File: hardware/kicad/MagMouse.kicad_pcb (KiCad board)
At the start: 4 copper layers, 50 x 95 mm, 183 parts, among them J1 TYPE-C-31-M-12, J2 COIL_L, J3 COIL_M, J4 COIL_R, Q1 2N7002, Q2 2N7002, Q3 2N7002, SW1 RESET, SW2 BOOT, U1 TPD2EUSB30DRTR, U10 ADS7038IRTER, U11 TUSB320LAIRWBR, U12 TPS259470LRPWR, U13 TPS259470LRPWR, U14 SN74LVC2G04DCKR, U15 SN74LVC1G123DCUR, U16 SN74LVC08APWR, U17 SN74LVC08APWR, U18 SN74LVC08APWR, U19 TLV9001IDBVR, U2 TPS62162DSGR, U20 TPD2E2U06DCKR, U3 ESP32-S3-MINI-1-N8, U4 DRV8231ADSGR, U5 DRV8231ADSGR, U6 DRV8231ADSGR, U7 TMAG5253BA2IQDMRR, U8 TMAG5253BA2IQDMRR, U9 TMAG5253BA2IQDMRR

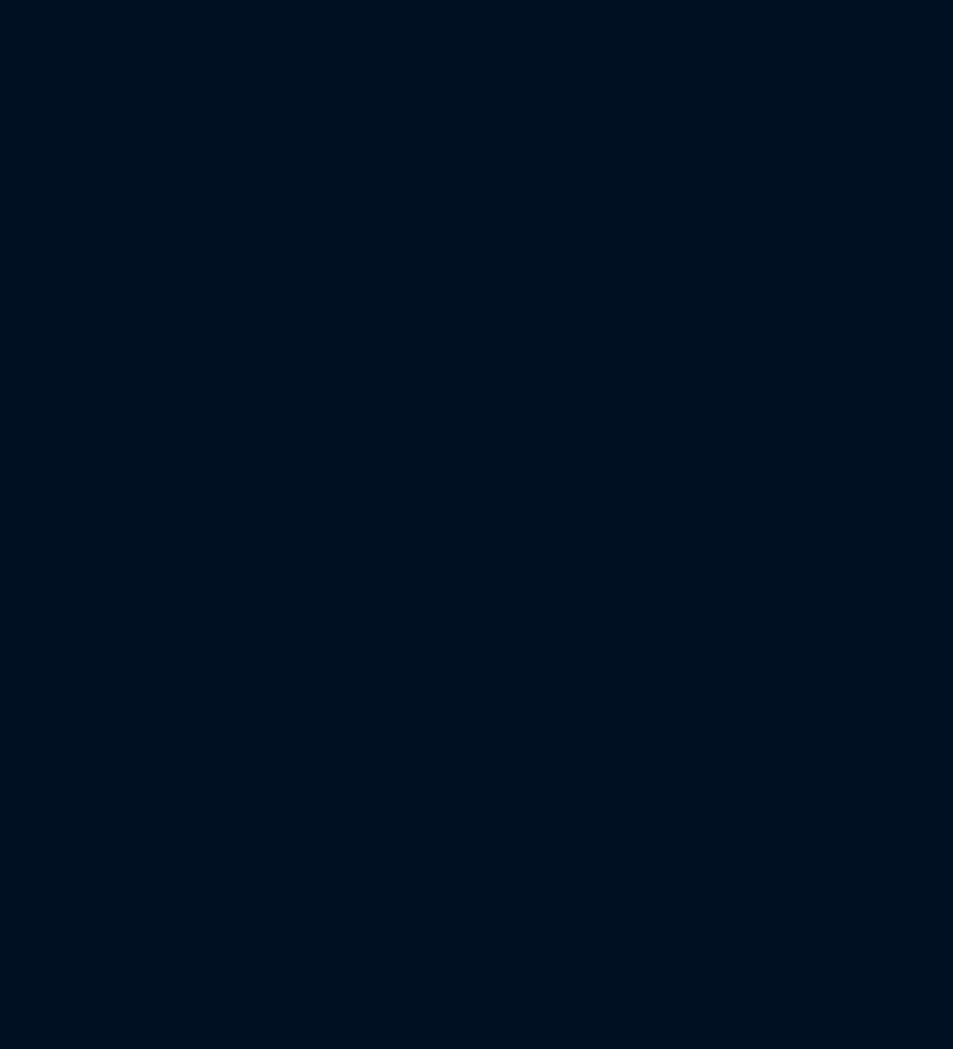
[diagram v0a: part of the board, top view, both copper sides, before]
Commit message: Add wheel control circuitry and autonomous regeneration brake
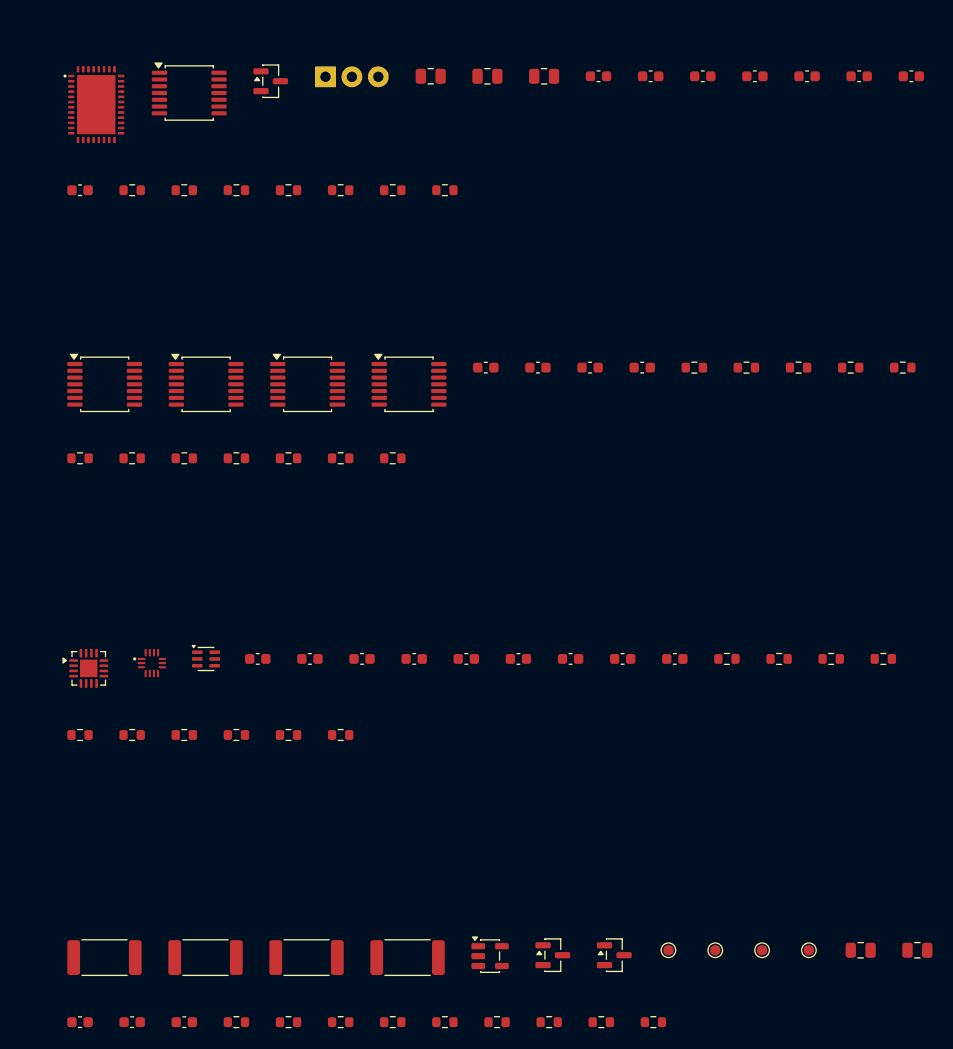
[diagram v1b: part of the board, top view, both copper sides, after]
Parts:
- added C41: 100nF, Capacitor_SMD:C_0603_1608Metric, F.Cu at (220.3, 111.2)
- added C42: 100nF, Capacitor_SMD:C_0603_1608Metric, F.Cu at (225.3, 111.2)
- added C43: 100nF, Capacitor_SMD:C_0603_1608Metric, F.Cu at (230.4, 111.2)
- added C44: 10uF/25V, Capacitor_SMD:C_0805_2012Metric, F.Cu at (204.2, 111.2)
- added C45: 10uF/25V, Capacitor_SMD:C_0805_2012Metric, F.Cu at (209.7, 111.2)
- added C46: 1uF/50V, Capacitor_SMD:C_0603_1608Metric, F.Cu at (235.4, 111.2)
- added C47: 47nF/50V, Capacitor_SMD:C_0603_1608Metric, F.Cu at (240.4, 111.2)
- added C48: 1uF/50V, Capacitor_SMD:C_0603_1608Metric, F.Cu at (245.4, 111.2)
- added C49: 100nF, Capacitor_SMD:C_0603_1608Metric, F.Cu at (250.4, 111.2)
- added C50: 22uF/25V, Capacitor_SMD:C_0805_2012Metric, F.Cu at (215.1, 111.2)
- added C51: 100nF, Capacitor_SMD:C_0603_1608Metric, F.Cu at (170.5, 122.2)
- added C52: 100nF, Capacitor_SMD:C_0603_1608Metric, F.Cu at (209.5, 139.2)
- added C53: 100nF, Capacitor_SMD:C_0603_1608Metric, F.Cu at (214.5, 139.2)
- added C54: 100nF, Capacitor_SMD:C_0603_1608Metric, F.Cu at (219.5, 139.2)
- added C55: 100nF, Capacitor_SMD:C_0603_1608Metric, F.Cu at (224.5, 139.2)
- added C56: 1uF/50V, Capacitor_SMD:C_0603_1608Metric, F.Cu at (187.6, 167.2)
- added C57: 1uF/50V, Capacitor_SMD:C_0603_1608Metric, F.Cu at (192.6, 167.2)
- added C58: 1uF/50V, Capacitor_SMD:C_0603_1608Metric, F.Cu at (197.6, 167.2)
- added C59: 22pF/50V, Capacitor_SMD:C_0603_1608Metric, F.Cu at (202.6, 167.2)
- added C60: 22pF/50V, Capacitor_SMD:C_0603_1608Metric, F.Cu at (207.6, 167.2)
- added C61: 22pF/50V, Capacitor_SMD:C_0603_1608Metric, F.Cu at (212.6, 167.2)
- added C62: 1uF/50V, Capacitor_SMD:C_0603_1608Metric, F.Cu at (217.6, 167.2)
- added C63: 1uF/50V, Capacitor_SMD:C_0603_1608Metric, F.Cu at (222.7, 167.2)
- added C64: 100nF, Capacitor_SMD:C_0603_1608Metric, F.Cu at (227.7, 167.2)
- added C65: 100nF, Capacitor_SMD:C_0603_1608Metric, F.Cu at (170.5, 202.2)
- added C66: 100nF, Capacitor_SMD:C_0603_1608Metric, F.Cu at (175.5, 202.2)
- added C67: 22pF/50V, Capacitor_SMD:C_0603_1608Metric, F.Cu at (180.5, 202.2)
- added C68: 10uF/25V, Capacitor_SMD:C_0805_2012Metric, F.Cu at (245.5, 195.2)
- added C69: 10uF/25V, Capacitor_SMD:C_0805_2012Metric, F.Cu at (251.0, 195.2)
- added J5: GB1806 phase wires, MagMouse:MotorWire_3x1mm_P2.54mm, F.Cu at (196.6, 111.3)
- added Q4: 2N7002, Package_TO_SOT_SMD:SOT-23, F.Cu at (188.8, 111.7)
- added Q5: AO3400A, Package_TO_SOT_SMD:SOT-23, F.Cu at (215.9, 195.7)
- added R100: 100k, Resistor_SMD:R_0603_1608Metric, F.Cu at (229.5, 139.2)
- added R101: 100k, Resistor_SMD:R_0603_1608Metric, F.Cu at (234.6, 139.2)
- added R102: 330R, Resistor_SMD:R_0603_1608Metric, F.Cu at (232.7, 167.2)
- added R103: 330R, Resistor_SMD:R_0603_1608Metric, F.Cu at (237.7, 167.2)
- added R104: 330R, Resistor_SMD:R_0603_1608Metric, F.Cu at (242.7, 167.2)
- added R105: 0R, Resistor_SMD:R_0603_1608Metric, F.Cu at (247.7, 167.2)
- added R106: 0R, Resistor_SMD:R_0603_1608Metric, F.Cu at (170.5, 174.6)
- added R107: 0R, Resistor_SMD:R_0603_1608Metric, F.Cu at (175.5, 174.6)
- added R108: 0R, Resistor_SMD:R_0603_1608Metric, F.Cu at (180.5, 174.6)
- added R109: 0R, Resistor_SMD:R_0603_1608Metric, F.Cu at (185.5, 174.6)
- added R110: 100k, Resistor_SMD:R_0603_1608Metric, F.Cu at (190.5, 174.6)
- added R111: 10k, Resistor_SMD:R_0603_1608Metric, F.Cu at (185.5, 202.2)
- added R112: 100k, Resistor_SMD:R_0603_1608Metric, F.Cu at (190.5, 202.2)
- added R113: 34.8k, Resistor_SMD:R_0603_1608Metric, F.Cu at (195.6, 202.2)
- added R114: 100k, Resistor_SMD:R_0603_1608Metric, F.Cu at (200.6, 202.2)
- added R115: 1M, Resistor_SMD:R_0603_1608Metric, F.Cu at (205.6, 202.2)
- added R116: 1M, Resistor_SMD:R_0603_1608Metric, F.Cu at (210.6, 202.2)
- added R117: 1M, Resistor_SMD:R_0603_1608Metric, F.Cu at (215.6, 202.2)
- added R119: 100R, Resistor_SMD:R_0603_1608Metric, F.Cu at (220.6, 202.2)
- added R120: 100k, Resistor_SMD:R_0603_1608Metric, F.Cu at (225.6, 202.2)
- added R121: 47R/2W, Resistor_SMD:R_2512_6332Metric, F.Cu at (172.9, 196.0)
- added R122: 47R/2W, Resistor_SMD:R_2512_6332Metric, F.Cu at (182.6, 196.0)
- added R123: 47R/2W, Resistor_SMD:R_2512_6332Metric, F.Cu at (192.3, 196.0)
- added R124: 47R/2W, Resistor_SMD:R_2512_6332Metric, F.Cu at (202.0, 196.0)
- added R125: 0R, Resistor_SMD:R_0603_1608Metric, F.Cu at (195.6, 174.6)
- added R81: 22R, Resistor_SMD:R_0603_1608Metric, F.Cu at (175.5, 122.2)
- added R82: 10k, Resistor_SMD:R_0603_1608Metric, F.Cu at (180.5, 122.2)
- added R83: 100k, Resistor_SMD:R_0603_1608Metric, F.Cu at (185.5, 122.2)
- added R84: 100k, Resistor_SMD:R_0603_1608Metric, F.Cu at (190.5, 122.2)
- added R86: 10k, Resistor_SMD:R_0603_1608Metric, F.Cu at (239.6, 139.2)
- added R87: 4.7k, Resistor_SMD:R_0603_1608Metric, F.Cu at (244.6, 139.2)
- added R88: 10k, Resistor_SMD:R_0603_1608Metric, F.Cu at (249.6, 139.2)
- added R89: 100k, Resistor_SMD:R_0603_1608Metric, F.Cu at (170.5, 148.0)
- added R90: 100k, Resistor_SMD:R_0603_1608Metric, F.Cu at (195.6, 122.2)
- added R91: 100k, Resistor_SMD:R_0603_1608Metric, F.Cu at (200.6, 122.2)
- added R92: 100k, Resistor_SMD:R_0603_1608Metric, F.Cu at (205.6, 122.2)
- added R94: 100k, Resistor_SMD:R_0603_1608Metric, F.Cu at (175.5, 148.0)
- added R95: 100k, Resistor_SMD:R_0603_1608Metric, F.Cu at (180.5, 148.0)
- added R96: 100k, Resistor_SMD:R_0603_1608Metric, F.Cu at (185.5, 148.0)
- added R97: 100k, Resistor_SMD:R_0603_1608Metric, F.Cu at (190.5, 148.0)
- added R98: 10k, Resistor_SMD:R_0603_1608Metric, F.Cu at (195.6, 148.0)
- added R99: 10k, Resistor_SMD:R_0603_1608Metric, F.Cu at (200.6, 148.0)
- added TP34: ACT_5V, TestPoint:TestPoint_Pad_D1.0mm, F.Cu at (227.1, 195.2)
- added TP35: BRAKE_REF, TestPoint:TestPoint_Pad_D1.0mm, F.Cu at (231.6, 195.2)
- added TP36: BRAKE_OUT, TestPoint:TestPoint_Pad_D1.0mm, F.Cu at (236.1, 195.2)
- added TP37: GND, TestPoint:TestPoint_Pad_D1.0mm, F.Cu at (240.6, 195.2)
- added U21: DRV8316RRGFR, MagMouse:Texas_RGF0040E, F.Cu at (172.1, 114.0)
- added U22: SN74LVC08APWR, Package_SO:TSSOP-14_4.4x5mm_P0.65mm, F.Cu at (181.0, 112.9)
- added U23: ADS7038IRTER, Package_DFN_QFN:WQFN-16-1EP_3x3mm_P0.5mm_EP1.68x1.68mm, F.Cu at (171.3, 168.2)
- added U24: SN74LVC125APWR, Package_SO:TSSOP-14_4.4x5mm_P0.65mm, F.Cu at (172.9, 140.9)
- added U25: SN74LVC125APWR, Package_SO:TSSOP-14_4.4x5mm_P0.65mm, F.Cu at (182.6, 140.9)
- added U26: SN74LVC125APWR, Package_SO:TSSOP-14_4.4x5mm_P0.65mm, F.Cu at (192.4, 140.9)
- added U27: MA735GGU-P, MagMouse:MPS_UTQFN14_2x2, F.Cu at (177.4, 167.7)
- added U28: TPS22919DCKR, Package_TO_SOT_SMD:SOT-363_SC-70-6, F.Cu at (182.6, 167.3)
- added U29: SN74LVC125APWR, Package_SO:TSSOP-14_4.4x5mm_P0.65mm, F.Cu at (202.1, 140.9)
- added U30: TLV1811DBVR, Package_TO_SOT_SMD:SOT-23-5, F.Cu at (209.9, 195.8)
- added U31: LM4040AIM3-2.5/NOPB, Package_TO_SOT_SMD:SOT-23, F.Cu at (221.9, 195.7)
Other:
- board text added: "STAGED 10 Wheel Driver - NOT PLACED"
- board text added: "STAGED 11 Wheel SPI - NOT PLACED"
- board text added: "STAGED 12 Wheel Feedback - NOT PLACED"
- board text added: "STAGED 13 Regeneration Brake - NOT PLACED"

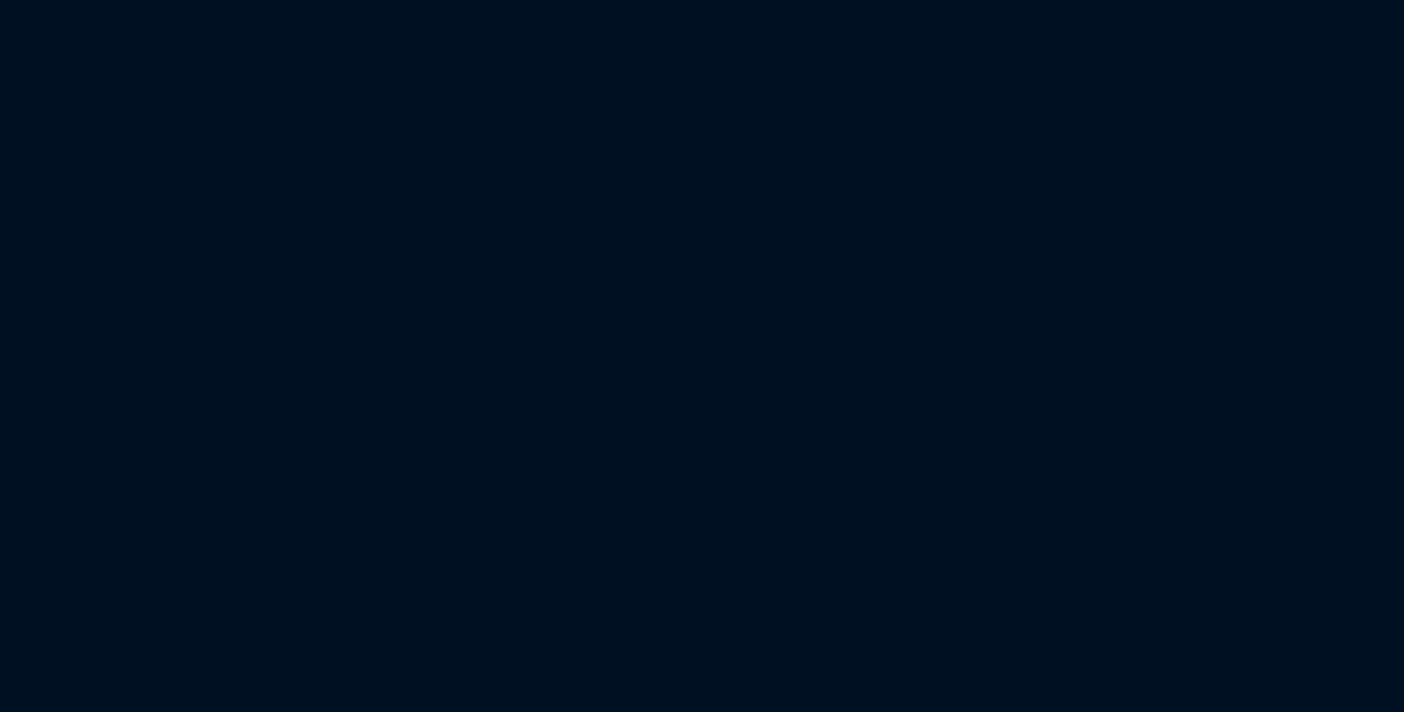
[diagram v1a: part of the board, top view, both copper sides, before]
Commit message: Add IMU and RGB circuits and document optical sourcing
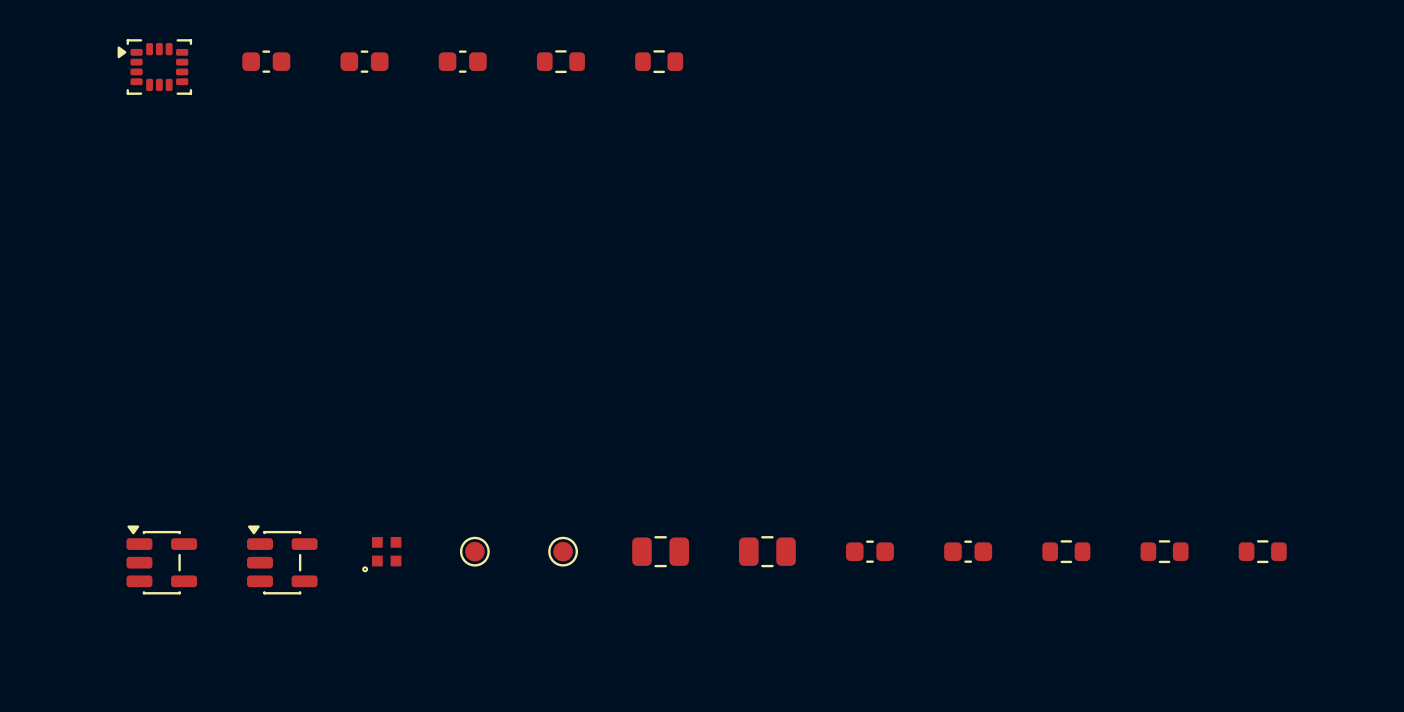
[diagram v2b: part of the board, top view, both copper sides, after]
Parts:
- added C70: 100nF, Capacitor_SMD:C_0603_1608Metric, F.Cu at (176.4, 51.2)
- added C71: 2.2uF/10V, Capacitor_SMD:C_0603_1608Metric, F.Cu at (181.4, 51.2)
- added C72: 10nF, Capacitor_SMD:C_0603_1608Metric, F.Cu at (186.4, 51.2)
- added C73: 10uF/25V, Capacitor_SMD:C_0805_2012Metric, F.Cu at (196.5, 76.2)
- added C74: 10uF/25V, Capacitor_SMD:C_0805_2012Metric, F.Cu at (202.0, 76.2)
- added C75: 100nF, Capacitor_SMD:C_0603_1608Metric, F.Cu at (207.2, 76.2)
- added C76: 100nF, Capacitor_SMD:C_0603_1608Metric, F.Cu at (212.2, 76.2)
- added D5: SK6805-EC15, MagMouse:OPSCO_SK6805_EC15, F.Cu at (182.6, 76.2)
- added R126: 10k, Resistor_SMD:R_0603_1608Metric, F.Cu at (191.4, 51.2)
- added R127: 10k, Resistor_SMD:R_0603_1608Metric, F.Cu at (196.4, 51.2)
- added R128: 330R, Resistor_SMD:R_0603_1608Metric, F.Cu at (217.2, 76.2)
- added R129: 100k, Resistor_SMD:R_0603_1608Metric, F.Cu at (222.2, 76.2)
- added R130: 10k, Resistor_SMD:R_0603_1608Metric, F.Cu at (227.2, 76.2)
- added TP38: RGB_5V, TestPoint:TestPoint_Pad_D1.0mm, F.Cu at (187.1, 76.2)
- added TP39: RGB_DIN, TestPoint:TestPoint_Pad_D1.0mm, F.Cu at (191.6, 76.2)
- added U32: ICM-42688-P, Package_LGA:LGA-14_3x2.5mm_P0.5mm_LayoutBorder3x4y, F.Cu at (171.0, 51.5)
- added U33: TPS7A2450DBVR, Package_TO_SOT_SMD:SOT-23-5, F.Cu at (171.1, 76.8)
- added U34: SN74LV1T34DBVR, Package_TO_SOT_SMD:SOT-23-5, F.Cu at (177.2, 76.8)
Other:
- board text added: "STAGED 14 IMU - NOT PLACED"
- board text added: "STAGED 15 RGB Status - NOT PLACED"

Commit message: Add PMW3360 optical circuitry and PCB-first mechanical datum
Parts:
- added C77: 10uF/25V, Capacitor_SMD:C_0805_2012Metric, F.Cu at (72.5, 41.2)
- added C78: 10uF/25V, Capacitor_SMD:C_0805_2012Metric, F.Cu at (78.0, 41.2)
- added C79: 1nF/50V, Capacitor_SMD:C_0603_1608Metric, F.Cu at (83.2, 41.2)
- added C80: 100nF, Capacitor_SMD:C_0603_1608Metric, F.Cu at (87.6, 66.2)
- added C81: 2.2uF/10V, Capacitor_SMD:C_0603_1608Metric, F.Cu at (88.2, 41.2)
- added C82: 2.2uF/10V, Capacitor_SMD:C_0603_1608Metric, F.Cu at (93.2, 41.2)
- added C83: 100nF, Capacitor_SMD:C_0603_1608Metric, F.Cu at (98.2, 41.2)
- added C84: 4.7uF/10V, Capacitor_SMD:C_0603_1608Metric, F.Cu at (103.2, 41.2)
- added C85: 100nF, Capacitor_SMD:C_0603_1608Metric, F.Cu at (108.3, 41.2)
- added C86: 100nF, Capacitor_SMD:C_0603_1608Metric, F.Cu at (92.6, 66.2)
- added C87: 100nF, Capacitor_SMD:C_0603_1608Metric, F.Cu at (97.6, 66.2)
- added R131: 10k, Resistor_SMD:R_0603_1608Metric, F.Cu at (102.6, 66.2)
- added R132: 39R, Resistor_SMD:R_0603_1608Metric, F.Cu at (113.3, 41.2)
- added R133: 100k, Resistor_SMD:R_0603_1608Metric, F.Cu at (107.6, 66.2)
- added R134: 100k, Resistor_SMD:R_0603_1608Metric, F.Cu at (112.6, 66.2)
- added R135: 10k, Resistor_SMD:R_0603_1608Metric, F.Cu at (117.6, 66.2)
- added R136: 100k, Resistor_SMD:R_0603_1608Metric, F.Cu at (122.6, 66.2)
- added TP40: OPT_3V3, TestPoint:TestPoint_Pad_D1.0mm, F.Cu at (58.5, 41.2)
- added TP41: OPT_1V9, TestPoint:TestPoint_Pad_D1.0mm, F.Cu at (63.0, 41.2)
- added TP42: OPT_VDDPIX, TestPoint:TestPoint_Pad_D1.0mm, F.Cu at (67.5, 41.2)
- added TP43: OPT_RESET_N, TestPoint:TestPoint_Pad_D1.0mm, F.Cu at (82.8, 66.2)
- added U35: PMW3360DM-T2QU, MagMouse:PixArt_PMW3360DM_T2QU, F.Cu at (125.5, 157.5)
- added U36: TLV75519PDBVR, Package_TO_SOT_SMD:SOT-23-5, F.Cu at (47.1, 41.8)
- added U37: SN74LVC125APWR, Package_SO:TSSOP-14_4.4x5mm_P0.65mm, F.Cu at (69.5, 67.9)
- added U38: TPS22918DBVR, Package_TO_SOT_SMD:SOT-23-6, F.Cu at (53.2, 41.8)
- added U39: SN74LVC1G125DBVR, Package_TO_SOT_SMD:SOT-23-5, F.Cu at (77.5, 66.8)
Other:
- board text added: "LENS SPACE 20 x 22 BELOW PCB - PROVISIONAL"
- board text added: "OPTICAL CENTRE SAMPLE FIT PENDING"
- board text added: "STAGED 16 Optical Power - NOT PLACED"
- board text added: "STAGED 17 Optical Support - U35 ON BOARD"
- board text removed: "PAW3950 / LENS OPTICAL RESERVE NO CUTOUT YET"
